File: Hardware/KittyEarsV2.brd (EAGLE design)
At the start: 50 x 34 mm, 27 parts, among them J1 455-1750-1-ND, J2 AVR_SPI_PROG_3X2TESTPOINTS, Q1 8/16/20MHz, U1 ATMEGA328, U2 MIC5205

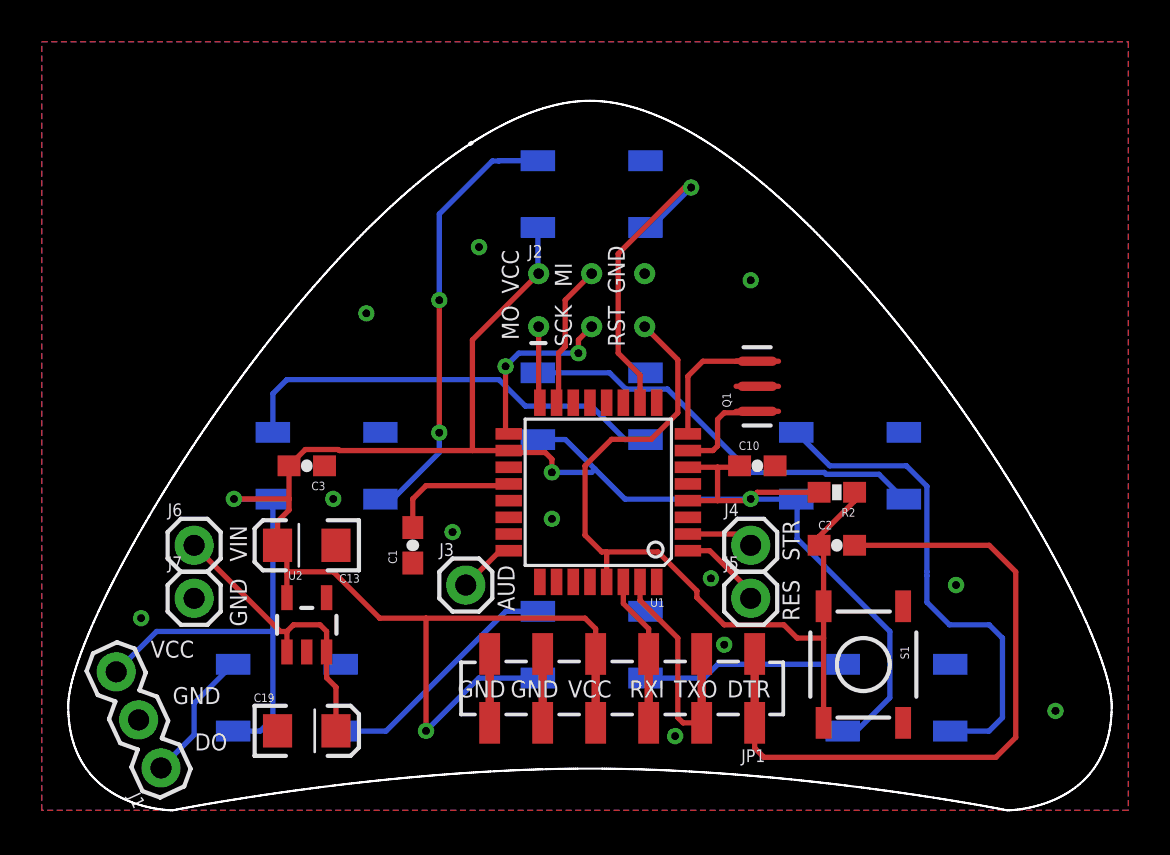
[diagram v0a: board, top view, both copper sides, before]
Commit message: Adding sketch fr new kitty ears
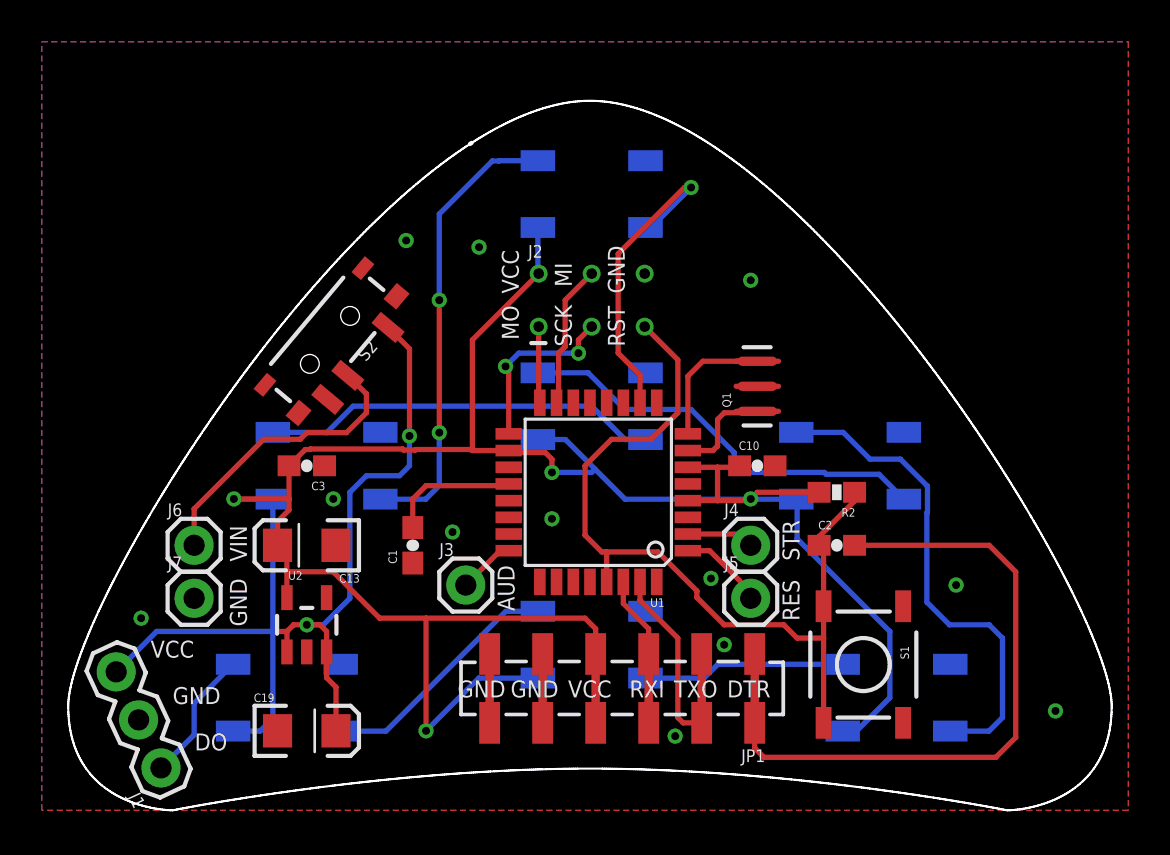
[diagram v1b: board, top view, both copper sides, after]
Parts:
- added S2: (no value), SparkFun-Switches:SWITCH_SPST_SMD_A
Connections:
- new net VIN: J6.1, S2.2
- net RAW: now also S2.3; no longer J6.1
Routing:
- net VIN: track 0.00 -> 14.1 mm
- net RAW: track 14.3 -> 26.7 mm, vias 0 -> 2
- net N$6: track 21.2 -> 19.0 mm
- net N$5: track 21.2 -> 21.9 mm
